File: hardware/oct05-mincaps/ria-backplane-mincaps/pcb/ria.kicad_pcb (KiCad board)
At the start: 4 copper layers, 50 x 69.5 mm, 69 parts

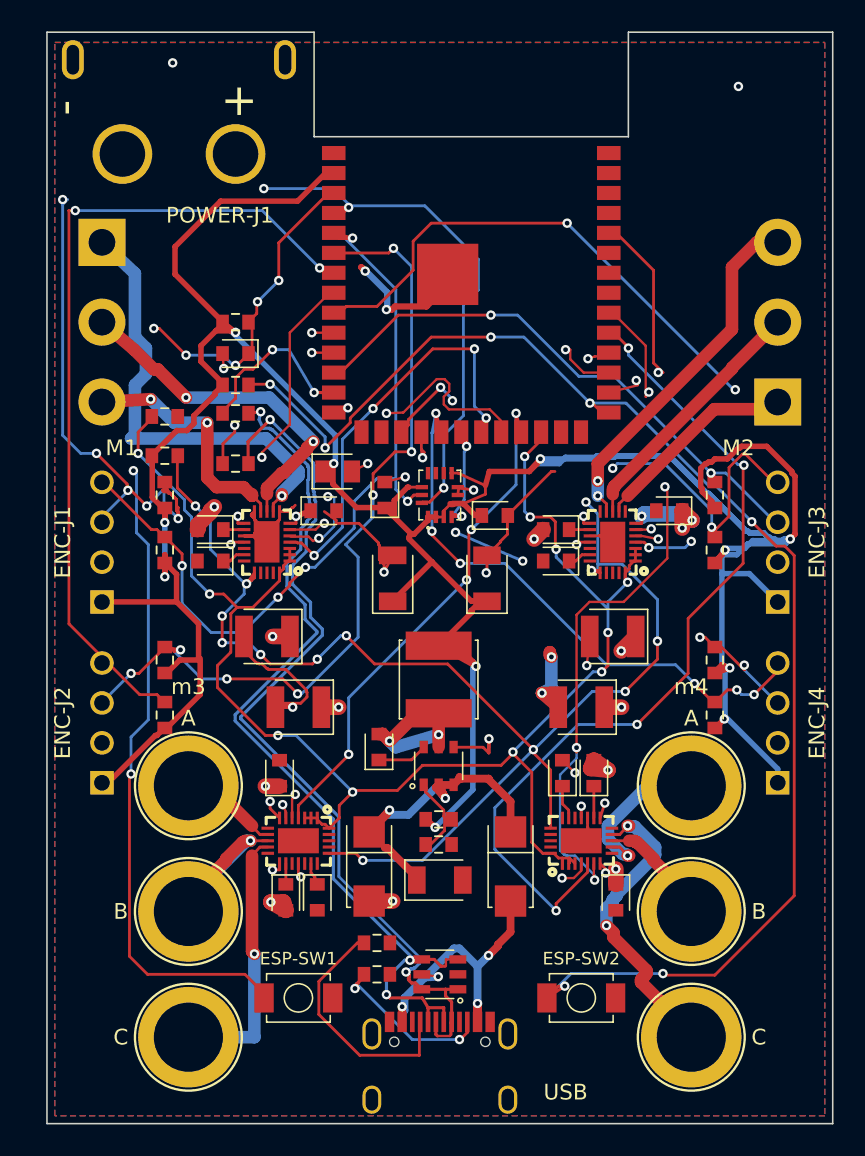
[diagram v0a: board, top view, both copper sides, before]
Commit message: value engineer capacitor sourcing and use available regulator
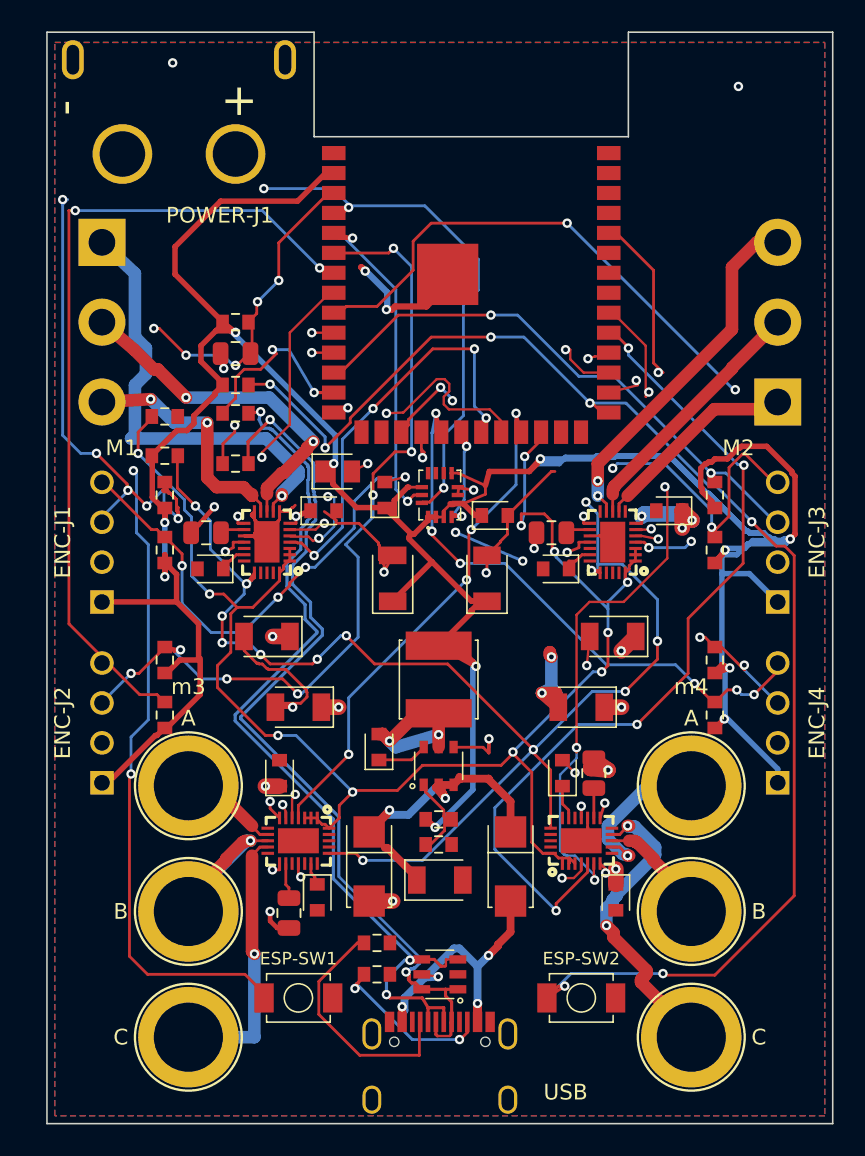
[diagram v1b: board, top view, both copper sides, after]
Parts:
- ESP-C3: footprint ria:ESP-C3 -> ria:C_0805_2012Metric
- MOTOR1-C2: footprint ria:MOTOR1-C2 -> ria:C_0805_2012Metric
- MOTOR1-C5: value 10uF -> 22uF; footprint ria:MOTOR1-C5 -> ria:C_1206_3216Metric
- MOTOR2-C2: footprint ria:MOTOR2-C2 -> ria:C_0805_2012Metric
- MOTOR2-C5: value 10uF -> 22uF; footprint ria:MOTOR2-C5 -> ria:C_1206_3216Metric
- MOTOR3-C2: footprint ria:MOTOR3-C2 -> ria:C_0805_2012Metric
- MOTOR3-C5: value 10uF -> 22uF; footprint ria:MOTOR3-C5 -> ria:C_1206_3216Metric
- MOTOR4-C2: footprint ria:MOTOR4-C2 -> ria:C_0805_2012Metric
- MOTOR4-C5: value 10uF -> 22uF; footprint ria:MOTOR4-C5 -> ria:C_1206_3216Metric
- POWER-U1: value AP63300WU-7 -> AP63301WU-7
- moved MOTOR3-C2 1.02 mm to (90.4, 126.6), turned to -90 degrees
- moved MOTOR1-C6 0.50 mm to (85.4, 104.7)
- moved MOTOR2-C6 0.50 mm to (107.4, 104.7)
- moved MOTOR2-C2 0.36 mm to (107.1, 102.4), turned to 180 degrees
- moved MOTOR1-C2 0.34 mm to (85.1, 102.4), turned to 180 degrees
- turned MOTOR1-C5 to 180 degrees
- turned MOTOR2-C5 to 180 degrees
- turned MOTOR3-C5 to 180 degrees
- turned MOTOR4-C2 to 90 degrees
- turned MOTOR4-C5 to 180 degrees
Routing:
- net MOTOR_ENABLE: track 96.0 -> 97.7 mm
- net BAT: track 33.0 -> 34.7 mm
- net MOTOR3_VCP: track 1.35 -> 2.28 mm
- net MOTOR2_V3P3: track 1.22 -> 1.72 mm
- net MOTOR1_V3P3: track 1.22 -> 1.72 mm
- net ESP_USB_DM: track 11.2 -> 11.7 mm
